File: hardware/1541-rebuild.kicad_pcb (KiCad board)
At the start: 2 copper layers, 23 parts, among them CON1 SD_Card, IC1 ATMEGA1284P-P, P1 1541_CN3, P2 1541_CN4_PIN7_[MOTOR], P3 VIA_PIN_1-20, P4 DIL40, P5 VIA_PIN_21-40, X1 20Mhz

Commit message: diverese Sachen geändert
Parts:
- removed P5: VIA_PIN_21-40, pin_header:pin_header_1x20_smd
- added SW1: SW_PUSH, Buttons_Switches_THT:SW_PUSH-12mm, F.Cu at (93.9, 120.4)
- added SW2: SW_PUSH, Buttons_Switches_THT:SW_PUSH-12mm, F.Cu at (111.0, 120.4)
- added SW3: SW_PUSH, Buttons_Switches_THT:SW_PUSH-12mm, F.Cu at (128.1, 120.4)
- C1, C2, C3: footprint Capacitors_ThroughHole:C_Disc_D6_P5 -> Capacitors_THT:C_Disc_D3_P2.5
- CON1: moved to F.Cu
- DS1: footprint WC1602A -> Pin_Headers:Pin_Header_Straight_1x16
- P1: value 1541_CN3 -> ISP; footprint Socket_Strips:Socket_Strip_Straight_1x06 -> Pin_Headers:Pin_Header_Straight_2x03
- P2: value 1541_CN4_PIN7_[MOTOR] -> VIA_PIN_1-20; footprint Pin_Headers:Pin_Header_Straight_1x01 -> Pin_Headers:Pin_Header_Straight_1x20; moved to B.Cu
- P3: value VIA_PIN_1-20 -> DIL40; footprint pin_header:pin_header_1x20_smd -> Housings_DIP:DIP-40_W15.24mm_LongPads; moved to F.Cu
- P4: value DIL40 -> VIA_PIN_21-40; footprint Housings_DIP:DIP-40_W15.24mm_LongPads -> Pin_Headers:Pin_Header_Straight_1x20; moved to B.Cu
- R2, R3: value 3,3k -> 1,8k
- R6, R7: value 1,8k -> 3,3k
- X1: footprint Oscillator-Modules:OSCILLATOR_KXO-200_LargePads -> Oscillators:KXO-200_LargePads
- moved C3 223.3 mm to (211.3, 104.5), turned to 180 degrees
- moved R3 188.4 mm to (130.7, 111.5)
- moved RV1 181.2 mm to (135.1, 69.0), turned to 270 degrees
- moved R1 172.0 mm to (85.6, 105.2), turned to 270 degrees
- moved C1 170.7 mm to (159.3, 102.6), turned to 90 degrees
- moved C2 163.5 mm to (136.4, 100.1)
- moved D1 154.0 mm to (85.6, 96.9), turned to 90 degrees
- moved R2 152.7 mm to (90.0, 91.2), turned to 90 degrees
- moved R6 150.9 mm to (82.4, 117.9), turned to 90 degrees
- moved R8 150.8 mm to (151.0, 65.2), turned to 180 degrees
- moved R4 140.9 mm to (98.9, 91.2), turned to 270 degrees
- moved R5 140.3 mm to (98.3, 105.2), turned to 90 degrees
- moved D2 130.9 mm to (81.2, 86.7), turned to 270 degrees
- moved R7 128.1 mm to (94.5, 91.2), turned to 270 degrees
- moved DS1 68.7 mm to (143.4, 68.3), turned to 90 degrees
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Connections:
- IC1 pad 24: Net-(IC1-Pad24) -> /VIA 6522 Sockel/MTR
- IC1 pad 26: Net-(IC1-Pad26) -> /VIA 6522 Sockel/WPS
- IC1 pad 27: Net-(IC1-Pad27) -> /VIA 6522 Sockel/OE
- IC1 pad 3: Net-(IC1-Pad3) -> GND
- IC1 pad 33: Net-(IC1-Pad33) -> /VIA 6522 Sockel/SPT0
- IC1 pad 34: Net-(IC1-Pad34) -> /VIA 6522 Sockel/STP1
- IC1 pad 4: Net-(IC1-Pad4) -> GND
- P1 pad 1: Net-(P1-Pad1) -> /SD Karte/MISO
- P1 pad 2: Net-(P1-Pad2) -> +5V
- P1 pad 3: Net-(IC1-Pad1) -> /SD Karte/SCK
- P1 pad 4: Net-(IC1-Pad3) -> /SD Karte/MOSI
- P1 pad 5: Net-(IC1-Pad2) -> Net-(IC1-Pad9)
- P1 pad 6: Net-(IC1-Pad4) -> GND
- P2 pad 1: Net-(IC1-Pad24) -> GND
- P4 pad 1: GND -> Net-(P3-Pad21)
- P4 pad 10: /VIA 6522 Sockel/STP1 -> Net-(P3-Pad30)
- P4 pad 11: /VIA 6522 Sockel/SPT0 -> Net-(P3-Pad31)
- P4 pad 12: /VIA 6522 Sockel/MTR -> Net-(P3-Pad32)
- P4 pad 13: /VIA 6522 Sockel/ACT -> Net-(P3-Pad33)
- P4 pad 14: /VIA 6522 Sockel/WPS -> Net-(P3-Pad34)
- P4 pad 15: /VIA 6522 Sockel/DS0 -> Net-(P3-Pad35)
- P4 pad 16: /VIA 6522 Sockel/DS1 -> Net-(P3-Pad36)
- P4 pad 17: /VIA 6522 Sockel/SYNC -> Net-(P3-Pad37)
- P4 pad 18: /VIA 6522 Sockel/NC -> Net-(P3-Pad38)
- P4 pad 19: /VIA 6522 Sockel/OE -> /VIA 6522 Sockel/SOE
- P4 pad 2: /VIA 6522 Sockel/PA0 -> Net-(P3-Pad22)
- P4 pad 20: +5V -> /VIA 6522 Sockel/BRDY
- P4 pad 3: /VIA 6522 Sockel/PA1 -> Net-(P3-Pad23)
- P4 pad 4: /VIA 6522 Sockel/PA2 -> Net-(P3-Pad24)
- P4 pad 5: /VIA 6522 Sockel/PA3 -> Net-(P3-Pad25)
- P4 pad 6: /VIA 6522 Sockel/PA4 -> Net-(P3-Pad26)
- P4 pad 7: /VIA 6522 Sockel/PA5 -> Net-(P3-Pad27)
- P4 pad 8: /VIA 6522 Sockel/PA6 -> Net-(P3-Pad28)
- P4 pad 9: /VIA 6522 Sockel/PA7 -> Net-(P3-Pad29)
- R2 pad 1: GND -> Net-(CON1-Pad1)
- R2 pad 2: Net-(CON1-Pad1) -> /SD Karte/SS
- R3 pad 1: GND -> Net-(CON1-Pad5)
- R3 pad 2: Net-(CON1-Pad2) -> /SD Karte/SCK
- R4 pad 2: Net-(CON1-Pad5) -> Net-(CON1-Pad1)
- R5 pad 1: Net-(CON1-Pad1) -> Net-(CON1-Pad2)
- R5 pad 2: /SD Karte/SS -> /SD Karte/MOSI
- R6 pad 1: Net-(CON1-Pad2) -> GND
- R6 pad 2: /SD Karte/MOSI -> Net-(CON1-Pad2)
- R7 pad 1: Net-(CON1-Pad5) -> GND
- R7 pad 2: /SD Karte/SCK -> Net-(CON1-Pad5)
- X1 pad 14: (no net) -> +5V
- X1 pad 7: (no net) -> GND
- X1 pad 8: +5V -> Net-(IC1-Pad13)
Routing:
- net +5V: track 29.0 -> 270.8 mm, vias 0 -> 6
- net Net-(IC1-Pad2): track 0.00 -> 138.5 mm, vias 0 -> 2
- net Net-(IC1-Pad1): track 0.00 -> 109.7 mm, vias 0 -> 2
- net Net-(IC1-Pad13): track 0.00 -> 109.1 mm, vias 0 -> 4
- net /VIA 6522 Sockel/SOE: track 5.08 -> 100.7 mm, vias 0 -> 2
- net /VIA 6522 Sockel/BRDY: track 10.2 -> 105.0 mm, vias 0 -> 1
- net Net-(CON1-Pad4): track 0.00 -> 71.0 mm, vias 0 -> 1
- net Net-(IC1-Pad9): track 0.00 -> 70.1 mm
- net /VIA 6522 Sockel/PA2: track 5.08 -> 73.3 mm, vias 0 -> 2
- net /VIA 6522 Sockel/PA0: track 5.08 -> 72.9 mm, vias 0 -> 2
- net /VIA 6522 Sockel/PA4: track 5.08 -> 72.5 mm, vias 0 -> 2
- net /VIA 6522 Sockel/PA6: track 5.08 -> 71.8 mm, vias 0 -> 2
- net /VIA 6522 Sockel/PA1: track 10.2 -> 73.6 mm, vias 0 -> 2
- net /VIA 6522 Sockel/PA7: track 10.2 -> 72.9 mm, vias 0 -> 2
- net /VIA 6522 Sockel/PA3: track 10.2 -> 72.9 mm, vias 0 -> 2
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- added copper zone on B.Cu, net GND
- added copper zone on F.Cu, net GND
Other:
- board outline added: 141.6 x 67.9 mm
- board text added: "1541-Rebuild Rev 1 by Thorsten Kattanek (C) DEZ.2016"

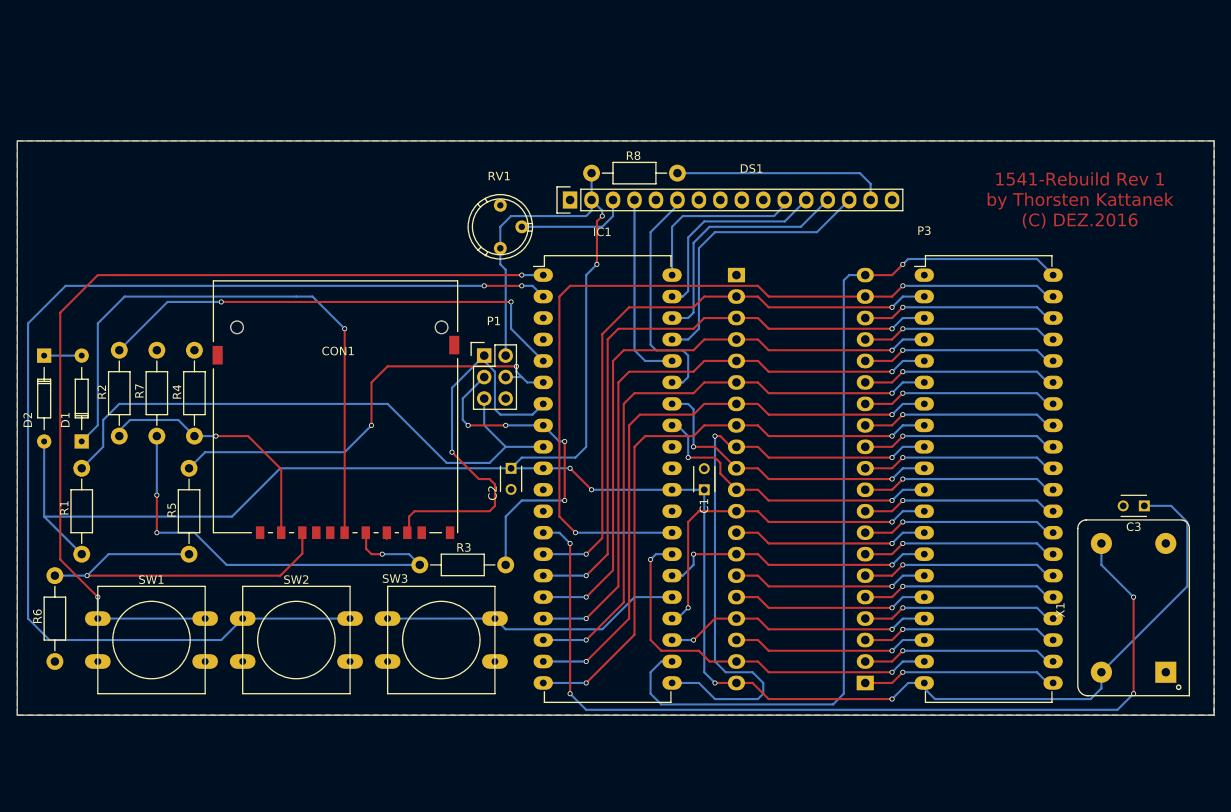
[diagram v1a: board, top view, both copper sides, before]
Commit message: Platine per Autorouter geroutet.
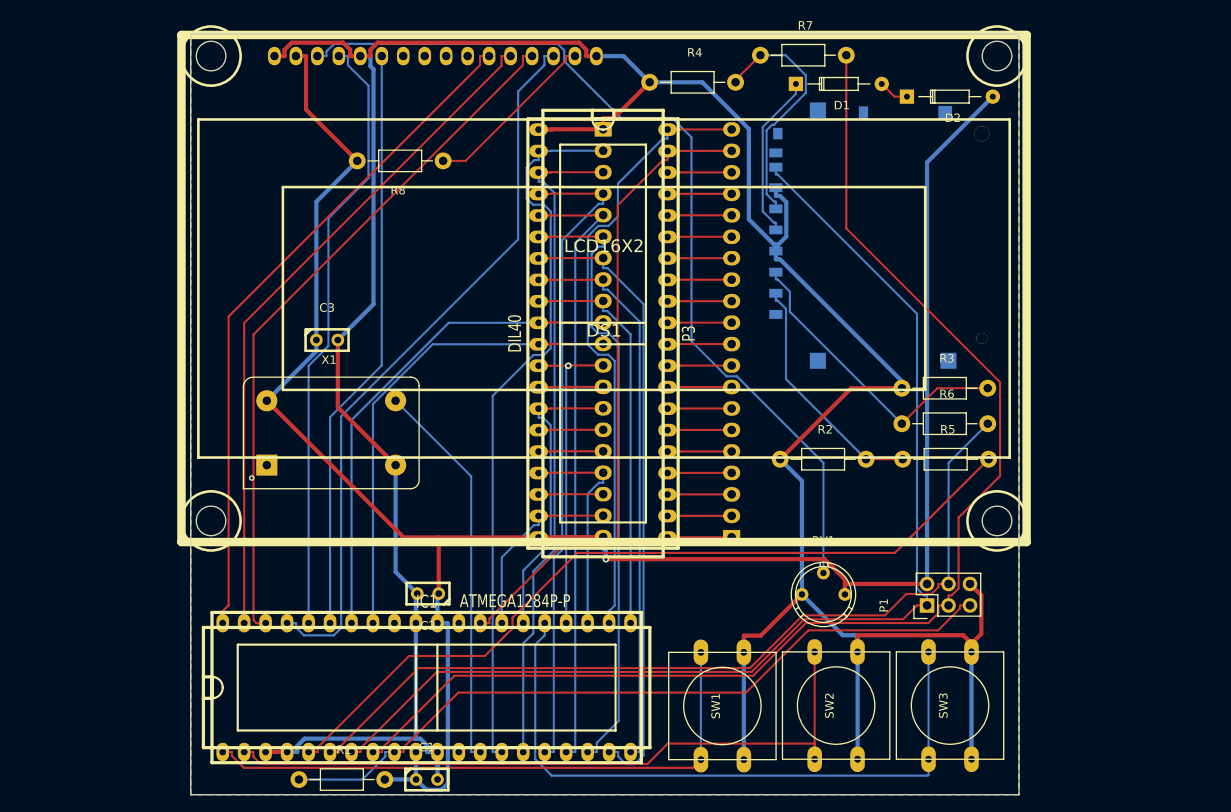
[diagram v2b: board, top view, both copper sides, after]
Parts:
- C1, C2, C3: footprint Capacitors_THT:C_Disc_D3_P2.5 -> w_capacitors:cnp_3mm_disc
- CON1: footprint Connect:SD_Card_Receptacle -> w_conn_misc:sd_socket; moved to B.Cu
- DS1: footprint Pin_Headers:Pin_Header_Straight_1x16 -> w_indicators:lcd_20x4
- IC1, P3: footprint Housings_DIP:DIP-40_W15.24mm_LongPads -> w_pth_circuits:dil_40-600_socket
- R2, R3: value 1,8k -> 3,3k
- R6, R7: value 3,3k -> 1,8k
- moved D2 106.6 mm to (183.2, 56.1), turned to 0 degrees
- moved R6 102.8 mm to (182.6, 94.8), turned to 0 degrees
- moved C3 98.7 mm to (114.6, 84.9), turned to 0 degrees
- moved X1 97.2 mm to (115.1, 95.9), turned to 0 degrees
- moved D1 94.5 mm to (170.1, 54.6), turned to 0 degrees
- moved R5 84.7 mm to (182.7, 99.0), turned to 0 degrees
- moved R7 81.8 mm to (165.9, 51.2), turned to 0 degrees
- moved R2 78.6 mm to (168.2, 99.0), turned to 0 degrees
- moved CON1 74.9 mm to (182.3, 72.6), turned to 270 degrees
- moved SW1 68.0 mm to (161.4, 128.2), turned to 90 degrees
- moved R4 65.2 mm to (152.8, 54.4), turned to 0 degrees
- moved SW2 64.3 mm to (174.9, 128.2), turned to 90 degrees
- moved SW3 60.7 mm to (188.3, 128.2), turned to 90 degrees
- moved P1 60.2 mm to (185.6, 116.3), turned to 90 degrees
- moved RV1 58.3 mm to (170.8, 115.0), turned to 0 degrees
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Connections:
- R2 pad 1: Net-(CON1-Pad1) -> GND
- R2 pad 2: /SD Karte/SS -> Net-(CON1-Pad1)
- R3 pad 1: Net-(CON1-Pad5) -> GND
- R3 pad 2: /SD Karte/SCK -> Net-(CON1-Pad2)
- R4 pad 2: Net-(CON1-Pad1) -> Net-(CON1-Pad5)
- R5 pad 1: Net-(CON1-Pad2) -> Net-(CON1-Pad1)
- R5 pad 2: /SD Karte/MOSI -> /SD Karte/SS
- R6 pad 1: GND -> Net-(CON1-Pad2)
- R6 pad 2: Net-(CON1-Pad2) -> /SD Karte/MOSI
- R7 pad 1: GND -> Net-(CON1-Pad5)
- R7 pad 2: Net-(CON1-Pad5) -> /SD Karte/SCK
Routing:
- net GND: track 0.84 -> 360.1 mm
- net /SD Karte/SCK: track 39.7 -> 151.5 mm, vias 4 -> 0
- net Net-(DS1-Pad3): track 13.2 -> 109.2 mm
- net /SD Karte/MISO: track 48.6 -> 135.2 mm, vias 1 -> 0
- net Net-(IC1-Pad13): track 109.1 -> 46.3 mm, vias 4 -> 0
- net /LCD Display/D0: track 20.7 -> 80.8 mm
- net /LCD Display/D1: track 24.3 -> 80.8 mm
- net Net-(IC1-Pad2): track 138.5 -> 82.1 mm, vias 2 -> 0
- net /LCD Display/D2: track 29.0 -> 82.6 mm
- net /LCD Display/D3: track 34.0 -> 86.4 mm
- net Net-(CON1-Pad4): track 71.0 -> 19.7 mm, vias 1 -> 0
- net /SD Karte/MOSI: track 52.9 -> 102.8 mm, vias 2 -> 0
- net /LCD Display/RS: track 22.8 -> 72.1 mm
- net Net-(IC1-Pad25): track 35.8 -> 78.5 mm
- net /LCD Display/EN: track 28.1 -> 69.6 mm
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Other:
- board size 141.6 x 67.9 mm -> 98 x 90 mm
- net class Default: via_dia 0.6 -> 0.8
- net class power added: clearance 0.2, trace_width 0.5, via_dia 0.8, via_drill 0.4
- board text removed: "1541-Rebuild Rev 1 by Thorsten Kattanek (C) DEZ.2016"

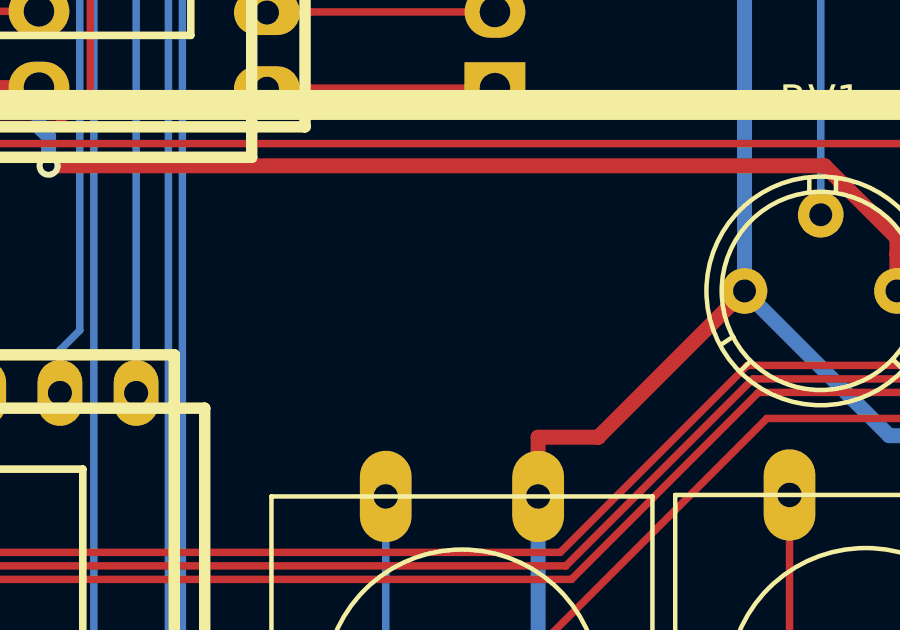
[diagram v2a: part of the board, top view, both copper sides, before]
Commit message: Logo in PCB eingefügt
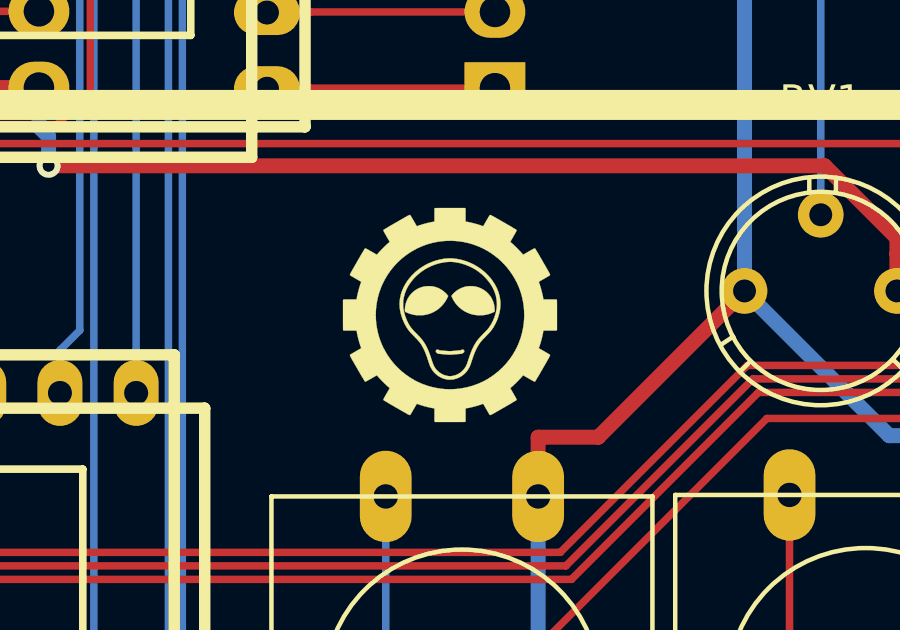
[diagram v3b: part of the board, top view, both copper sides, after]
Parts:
- added G***: LOGO, Logos:logo_01_7_1mm_fsilk, F.Cu at (161.0, 115.8)

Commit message: PCB Board gelöscht um mit älteren KiCad Versionen kompatibel zu sein.
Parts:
- removed C1, C2, C3: 100n, w_capacitors:cnp_3mm_disc
- removed CON1: SD_Card, w_conn_misc:sd_socket
- removed D1, D2: 1N4148, Diodes_ThroughHole:Diode_DO-35_SOD27_Horizontal_RM10
- removed DS1: LCD16X2, w_indicators:lcd_20x4
- removed G***: LOGO, Logos:logo_01_7_1mm_fsilk
- removed IC1: ATMEGA1284P-P, w_pth_circuits:dil_40-600_socket
- removed P1: ISP, Pin_Headers:Pin_Header_Straight_2x03
- removed P2: VIA_PIN_1-20, Pin_Headers:Pin_Header_Straight_1x20
- removed P3: DIL40, w_pth_circuits:dil_40-600_socket
- removed P4: VIA_PIN_21-40, Pin_Headers:Pin_Header_Straight_1x20
- removed R1: 10k, Resistors_ThroughHole:Resistor_Horizontal_RM10mm
- removed R2, R3, R4: 3,3k, Resistors_ThroughHole:Resistor_Horizontal_RM10mm
- removed R5, R6, R7: 1,8k, Resistors_ThroughHole:Resistor_Horizontal_RM10mm
- removed R8: 150, Resistors_ThroughHole:Resistor_Horizontal_RM10mm
- removed RV1: 10k, Potentiometers:Potentiometer_Bourns_3339P_Angular_ScrewUp
- removed SW1, SW2, SW3: SW_PUSH, Buttons_Switches_THT:SW_PUSH-12mm
- removed X1: 20Mhz, Oscillators:KXO-200_LargePads
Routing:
- net GND: track 360.1 -> 0.00 mm
- net +5V: track 241.8 -> 0.00 mm, vias 1 -> 0
- net /SD Karte/SCK: track 151.5 -> 0.00 mm
- net /SD Karte/MISO: track 135.2 -> 0.00 mm
- net Net-(DS1-Pad3): track 109.2 -> 0.00 mm
- net /SD Karte/MOSI: track 102.8 -> 0.00 mm
- net /SD Karte/SS: track 95.9 -> 0.00 mm
- net Net-(IC1-Pad9): track 88.8 -> 0.00 mm
- net /LCD Display/D3: track 86.4 -> 0.00 mm
- net /VIA 6522 Sockel/PA0: track 86.2 -> 0.00 mm
- net /LCD Display/D2: track 82.6 -> 0.00 mm
- net Net-(IC1-Pad2): track 82.1 -> 0.00 mm
- net /LCD Display/D1: track 80.8 -> 0.00 mm
- net /LCD Display/D0: track 80.8 -> 0.00 mm
- net /VIA 6522 Sockel/PA1: track 78.8 -> 0.00 mm
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- removed copper zone on B.Cu, net GND
- removed copper zone on F.Cu, net GND
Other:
- board outline removed
- net class Default: via_dia 0.8 -> 0.6
- net class power removed

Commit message: - Anordnung aller Bauteile (Problem noch mit SD-Slot) - Erstes PCB Layout mit Freeroute - Autorouter.
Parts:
- added C1: 100n, w_capacitors:cnp_3mm_disc, F.Cu at (161.3, 102.9)
- added C2: 100n, w_capacitors:cnp_3mm_disc, F.Cu at (154.9, 80.0)
- added C3: 100n, w_capacitors:cnp_3mm_disc, F.Cu at (114.3, 132.1)
- added CON1: SD_Card, w_conn_misc:sd_socket, F.Cu at (165.1, 61.0)
- added D1: 1N4148, Diodes_THT:D_DO-35_SOD27_P7.62mm_Horizontal, F.Cu at (144.8, 62.2)
- added D2: 1N4148, Diodes_THT:D_DO-35_SOD27_P7.62mm_Horizontal, F.Cu at (139.7, 54.6)
- added G***: LOGO, Logos:logo_01_10_7mm_fsilk, F.Cu at (116.8, 49.5)
- added IC1: ATMEGA1284P-P, w_pth_circuits:dil_40-600_socket, F.Cu at (154.9, 91.4)
- added J1: ISP, w_conn_strip:vasch_strip_3x2, F.Cu at (118.1, 71.1)
- added J2: KEYS, Pin_Headers:Pin_Header_Straight_1x04_Pitch2.54mm, F.Cu at (130.8, 104.1)
- added J3: EXT_5V, Pin_Headers:Pin_Header_Straight_1x02_Pitch2.54mm, F.Cu at (118.1, 59.7)
- added J4: RESET CONN, Pin_Headers:Pin_Header_Straight_1x02_Pitch2.54mm, F.Cu at (163.8, 134.6)
- added J5: PC7, Pin_Headers:Pin_Header_Straight_1x01_Pitch2.54mm, F.Cu at (160.0, 80.0)
- added J6: LCD Display, w_conn_strip:vasch_strip_5x2, F.Cu at (118.1, 94.0)
- added P1: VIA_PIN_1-20, Pin_Headers:Pin_Header_Straight_1x20_Pitch2.54mm, B.Cu at (179.1, 114.3)
- added P2: VIA-6522, w_pth_circuits:dil_40-600_socket, F.Cu at (154.9, 116.8)
- added P3: VIA_PIN_21-40, Pin_Headers:Pin_Header_Straight_1x20_Pitch2.54mm, B.Cu at (130.8, 129.5)
- added R1: 10k, Discret:R4-5, F.Cu at (172.7, 105.4)
- added R10: 150, Discret:R4-5, F.Cu at (118.1, 81.3)
- added R2: 3,3k, Discret:R4-5, F.Cu at (141.0, 45.7)
- added R3: 3,3k, Discret:R4-5, F.Cu at (129.5, 55.9)
- added R4: 3,3k, Discret:R4-5, F.Cu at (139.7, 72.4)
- added R5: 47k, Discret:R4-5, F.Cu at (125.7, 97.8)
- added R6: 47kR, Discret:R4-5, F.Cu at (148.6, 102.9)
- added R7: 1,8k, Discret:R4-5, F.Cu at (141.0, 50.8)
- added R8: 1,8k, Discret:R4-5, F.Cu at (129.5, 59.7)
- added R9: 1,8k, Discret:R4-5, F.Cu at (139.7, 67.3)
- added RV1: 10k, w_pth_resistors:trimmer_vishay_64w, F.Cu at (128.3, 72.4)
- added SW1: RESET, Buttons_Switches_THT:SW_PUSH_6mm_h5mm, F.Cu at (118.1, 130.8)
- added X1: 24Mhz, Oscillators:Oscillator_DIP-14_LargePads, F.Cu at (123.2, 124.5)
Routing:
- net GND: track 0.00 -> 291.3 mm
- net +5V: track 0.00 -> 200.9 mm, vias 0 -> 1
- net Net-(IC1-Pad9): track 0.00 -> 159.3 mm
- net /SD Karte/MISO: track 0.00 -> 72.4 mm, vias 0 -> 1
- net /SD Karte/SCK: track 0.00 -> 61.7 mm
- net /SD Karte/MOSI: track 0.00 -> 59.0 mm
- net /VIA 6522 Sockel/SYNC: track 0.00 -> 56.8 mm
- net Net-(IC1-Pad13): track 0.00 -> 54.8 mm
- net /VIA 6522 Sockel/SOE: track 0.00 -> 54.3 mm
- net /SD Karte/SS: track 0.00 -> 52.6 mm
- net /VIA 6522 Sockel/OE: track 0.00 -> 48.9 mm
- net /VIA 6522 Sockel/BRDY: track 0.00 -> 48.4 mm
- net Net-(IC1-Pad25): track 0.00 -> 45.2 mm
- net /VIA 6522 Sockel/MTR: track 0.00 -> 41.9 mm
- net /VIA 6522 Sockel/PA7: track 0.00 -> 41.8 mm
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- added copper zone on B.Cu, net GND
- added copper zone on F.Cu, net GND
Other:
- board outline added: 76.2 x 97.8 mm
- net class Default: trace_width 0.25 -> 0.3
- net class Power5V added: clearance 0.3, trace_width 0.6, via_dia 0.6, via_drill 0.4
- board text added: "1541-rebuild Rev.: 1.3.3"
- board text added: "24MHz"
- board text added: "ISP"
- board text added: "LCD"
- board text added: "von thorsten kattanek"
